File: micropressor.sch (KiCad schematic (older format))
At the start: 10 parts, among them IC1 PIC24FJ256GA702-I_SP, J1 Conn_01x06_Male, J5 Conn_01x06_Male, SW1 SW_Push

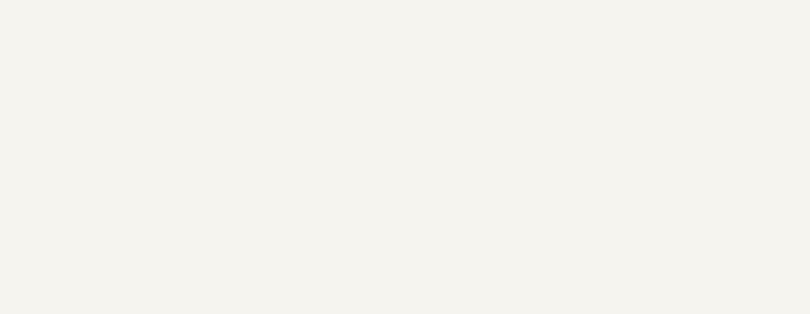
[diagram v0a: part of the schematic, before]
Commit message: Note added to fix SPI pin in next revision
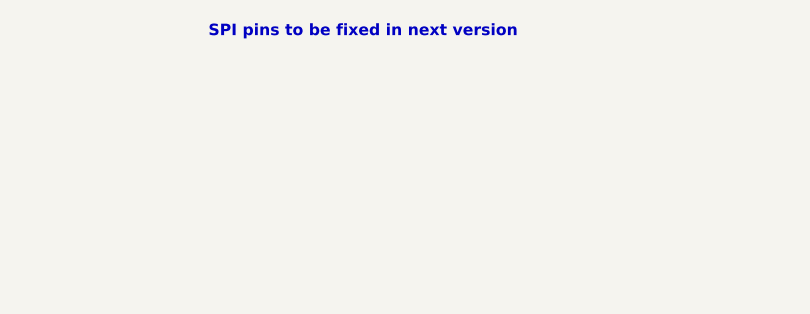
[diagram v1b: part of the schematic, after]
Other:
- note added: "SPI pins to be fixed in next version"
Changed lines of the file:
@@
 Wire Wire Line
 	3550 3450 3550 4100
+Text Notes 4650 1050 0    50   ~ 10
+SPI pins to be fixed in next version
 $EndSCHEMATC
